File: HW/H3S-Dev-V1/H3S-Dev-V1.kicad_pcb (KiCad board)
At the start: 2 copper layers, 85 x 56 mm, 69 parts, among them J1 USB_C_Receptacle_USB2.0_16P, J2 Conn_01x02, J3 Conn_Coaxial, J4 Conn_01x04, J5 Conn_01x04, Q1 DMP3099L, SW1 SW_Push, SW2 SW_Push, U1 Ra-01SH-P, U2 LTC4054ES5-4.2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

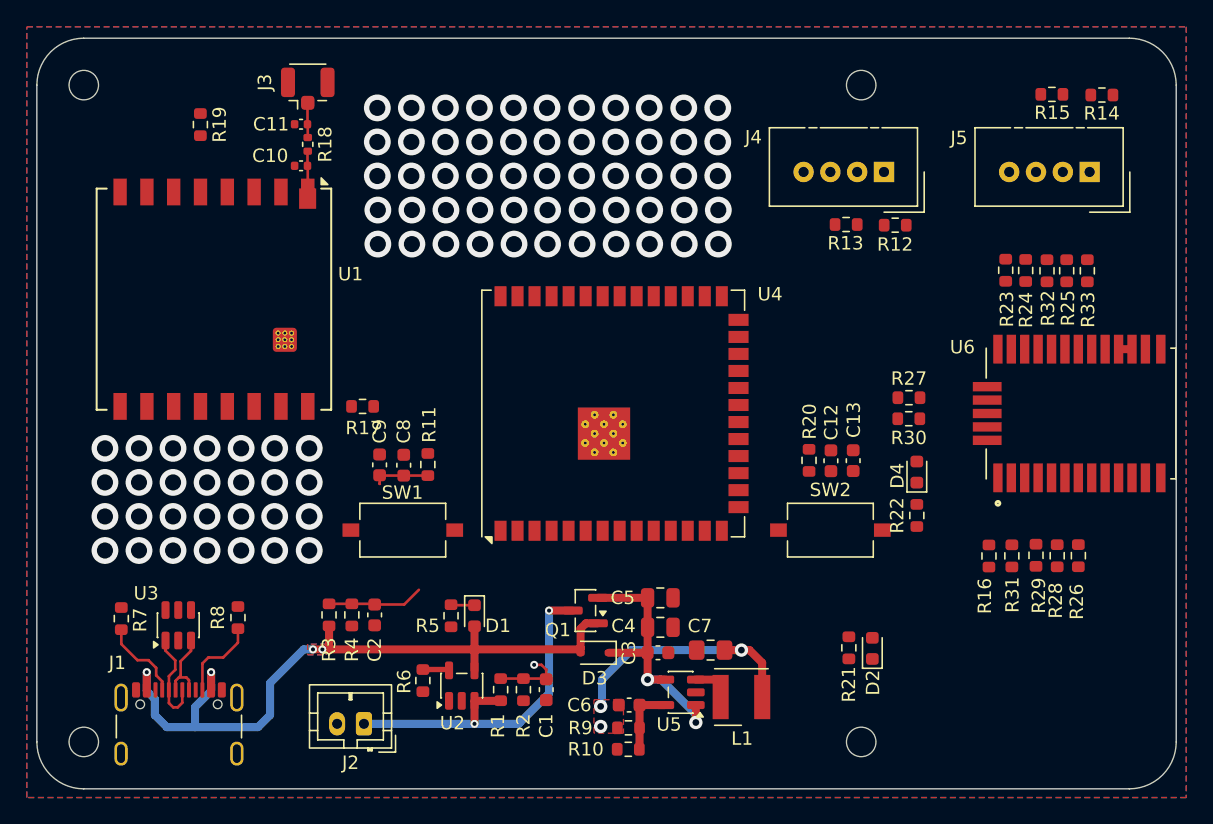
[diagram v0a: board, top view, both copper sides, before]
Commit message: LoRa intereface connected
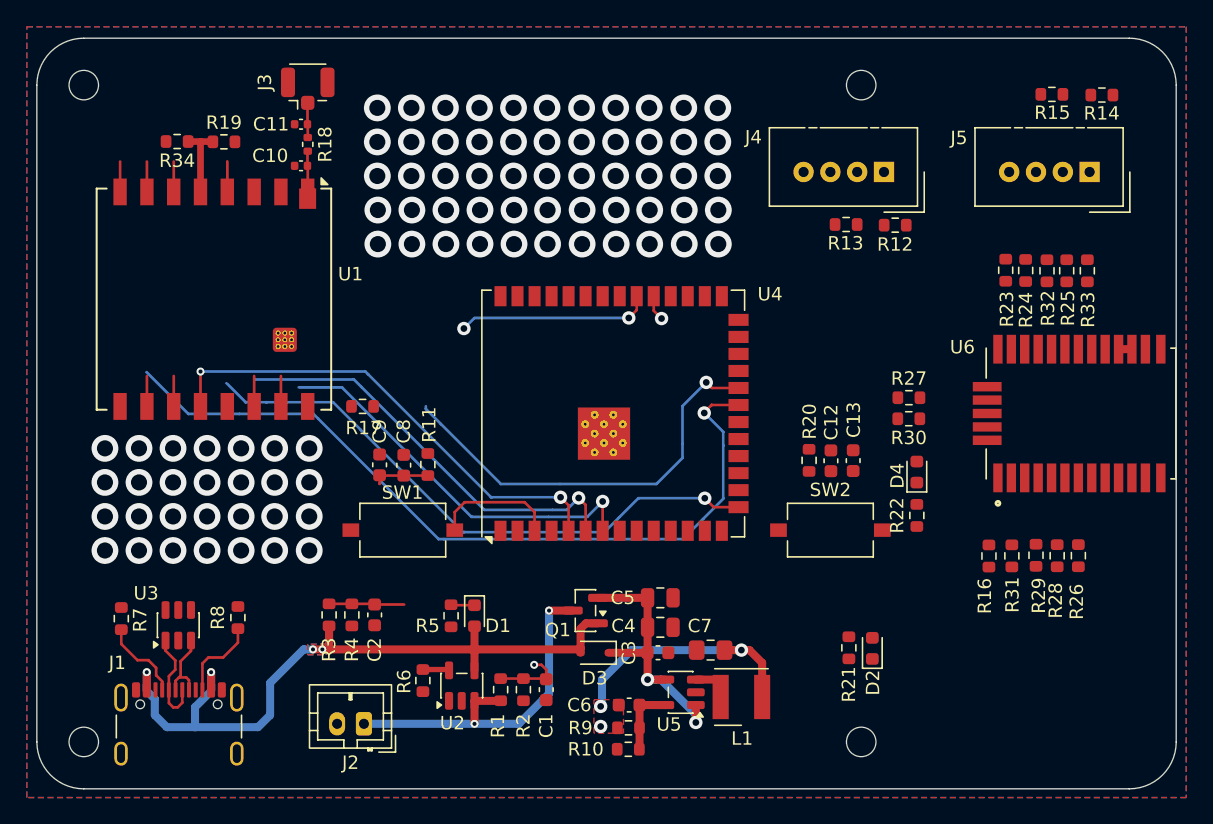
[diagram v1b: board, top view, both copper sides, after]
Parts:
- added R34: 0, Resistor_SMD:R_0603_1608Metric, F.Cu at (110.5, 81.7)
- moved R19 2.18 mm to (114.0, 81.7), turned to 0 degrees
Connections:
- R19 pad 1: VCC -> Net-(U1-VCCPA)
- R19 pad 2: Net-(U1-VCCPA) -> VCC
- U1 pad 6: /DIO0 -> /DIO1
- U1 pad 7: /DIO1 -> /DIO2
- U1 pad 8: /DIO2 -> /DIO3
- U4 pad 10: /DIO2 -> /L_BUSY
- U4 pad 21: /L_BUSY -> /L_RF_EN
- U4 pad 22: /L_RF_EN -> /DIO3
- U4 pad 8: /DIO0 -> /DIO2
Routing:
- net /L_RF_EN: track 0.00 -> 59.3 mm, vias 0 -> 1
- net /MISO: track 0.00 -> 44.1 mm, vias 0 -> 1
- net /SCK: track 0.00 -> 35.8 mm, vias 0 -> 2
- net /DIO3: track 0.00 -> 33.7 mm, vias 0 -> 1
- net /MOSI: track 0.00 -> 33.5 mm, vias 0 -> 1
- net /~{SS}: track 0.00 -> 31.7 mm, vias 0 -> 1
- net /V5_SENSE: track 7.18 -> 20.1 mm, vias 0 -> 2
- net /~{ESP_EN}: track 4.34 -> 13.6 mm
- net Net-(U1-VCCPA): track 0.00 -> 5.56 mm
- net Net-(U1-RF_EN): track 0.00 -> 2.27 mm
- net /~{L_RST}: track 0.00 -> 2.27 mm
- net /L_BUSY: track 0.00 -> 2.27 mm
- net /DIO2: track 0.00 -> 2.27 mm
- net /DIO1: track 0.00 -> 2.27 mm
- net /BAT_SENSE: track 5.19 -> 7.13 mm, vias 1 -> 2
